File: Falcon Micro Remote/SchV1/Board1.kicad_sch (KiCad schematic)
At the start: 41 parts, among them J41 Conn_01x02_Male, J51 Conn_01x03_Male, SW31 SW_Push, SW51 SW_Push, SW61 SW_Push, SW62 SW_Push, SW63 SW_Push, SW64 SW_Push, SW71 SW_Push, SW72 SW_Push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

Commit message: Made modifications to sch and brd files
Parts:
- D41: footprint (none) -> Diode_SMD:D_SMA
- J41: footprint (none) -> Connector_PinSocket_2.54mm:PinSocket_1x02_P2.54mm_Vertical
- R41, R42: footprint (none) -> Resistor_SMD:R_0402_1005Metric
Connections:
- net B: no longer U2.28 (IO17)
- net F: no longer U2.27 (IO16)
- net L: no longer U2.30 (IO18)
- net L1: no longer R74.1, SW74.2
- net L2: no longer R75.1, SW75.2
- net R: no longer U2.31 (IO19)
- net R1: no longer R71.1, SW71.2
- net LT renamed 23
- net 23: now also U2.37 (IO23)
- net R2 renamed 17
- net 17: now also U2.28 (IO17); no longer U2.36 (IO22)
- net RT renamed 18
- net 18: now also U2.30 (IO18); no longer U2.37 (IO23)
- new net 16: R71.1, SW71.2, U2.27 (IO16)
- new net 19: R74.1, SW74.2, U2.31 (IO19)
- new net 22: R75.1, SW75.2, U2.36 (IO22)
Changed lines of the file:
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@@
     )
   )
-  (global_label "R2" (shape input) (at 60.96 118.745 0) (fields_autoplaced)
-    (effects (font (size 1.27 1.27)) (justify left))
-    (property "Intersheet References" "${INTERSHEET_REFS}" (id 0) (at 65.8526 118.6656 0)
-      (effects (font (size 1.27 1.27)) (justify left) hide)
-    )
-  )
-  (global_label "LT" (shape input) (at 264.16 123.19 0) (fields_autoplaced)
-    (effects (font (size 1.27 1.27)) (justify left))
-    (property "Intersheet References" "${INTERSHEET_REFS}" (id 0) (at 268.5688 123.1106 0)
+  (global_label "22" (shape input) (at 60.96 118.745 0) (fields_autoplaced)
+    (effects (font (size 1.27 1.27)) (justify left))
+    (property "Intersheet References" "${INTERSHEET_REFS}" (id 0) (at 65.7921 118.6656 0)
+      (effects (font (size 1.27 1.27)) (justify left) hide)
+    )
+  )
+  (global_label "23" (shape input) (at 264.16 123.19 0) (fields_autoplaced)
+    (effects (font (size 1.27 1.27)) (justify left))
+    (property "Intersheet References" "${INTERSHEET_REFS}" (id 0) (at 268.9921 123.1106 0)
       (effects (font (size 1.27 1.27)) (justify left) hide)
     )
@@
     )
   )
-  (global_label "R2" (shape input) (at 264.16 53.34 0) (fields_autoplaced)
-    (effects (font (size 1.27 1.27)) (justify left))
-    (property "Intersheet References" "${INTERSHEET_REFS}" (id 0) (at 269.0526 53.2606 0)
+  (global_label "17" (shape input) (at 264.16 53.34 0) (fields_autoplaced)
+    (effects (font (size 1.27 1.27)) (justify left))
+    (property "Intersheet References" "${INTERSHEET_REFS}" (id 0) (at 268.9921 53.2606 0)
       (effects (font (size 1.27 1.27)) (justify left) hide)
     )
@@
     )
   )
-  (global_label "RT" (shape input) (at 264.16 71.755 0) (fields_autoplaced)
-    (effects (font (size 1.27 1.27)) (justify left))
-    (property "Intersheet References" "${INTERSHEET_REFS}" (id 0) (at 268.8107 71.6756 0)
-      (effects (font (size 1.27 1.27)) (justify left) hide)
-    )
-  )
-  (global_label "F" (shape input) (at 60.96 106.045 0) (fields_autoplaced)
-    (effects (font (size 1.27 1.27)) (justify left))
-    (property "Intersheet References" "${INTERSHEET_REFS}" (id 0) (at 64.4617 105.9656 0)
+  (global_label "18" (shape input) (at 264.16 71.755 0) (fields_autoplaced)
+    (effects (font (size 1.27 1.27)) (justify left))
+    (property "Intersheet References" "${INTERSHEET_REFS}" (id 0) (at 268.9921 71.6756 0)
+      (effects (font (size 1.27 1.27)) (justify left) hide)
+    )
+  )
+  (global_label "16" (shape input) (at 60.96 106.045 0) (fields_autoplaced)
+    (effects (font (size 1.27 1.27)) (justify left))
+    (property "Intersheet References" "${INTERSHEET_REFS}" (id 0) (at 65.7921 105.9656 0)
       (effects (font (size 1.27 1.27)) (justify left) hide)
     )
@@
     )
   )
-  (global_label "RT" (shape input) (at 60.96 121.285 0) (fields_autoplaced)
-    (effects (font (size 1.27 1.27)) (justify left))
-    (property "Intersheet References" "${INTERSHEET_REFS}" (id 0) (at 65.6107 121.2056 0)
+  (global_label "23" (shape input) (at 60.96 121.285 0) (fields_autoplaced)
+    (effects (font (size 1.27 1.27)) (justify left))
+    (property "Intersheet References" "${INTERSHEET_REFS}" (id 0) (at 65.7921 121.2056 0)
       (effects (font (size 1.27 1.27)) (justify left) hide)
     )
@@
     )
   )
-  (global_label "L1" (shape input) (at 264.16 88.9 0) (fields_autoplaced)
-    (effects (font (size 1.27 1.27)) (justify left))
-    (property "Intersheet References" "${INTERSHEET_REFS}" (id 0) (at 268.8107 88.8206 0)
+  (global_label "19" (shape input) (at 264.16 88.9 0) (fields_autoplaced)
+    (effects (font (size 1.27 1.27)) (justify left))
+    (property "Intersheet References" "${INTERSHEET_REFS}" (id 0) (at 268.9921 88.8206 0)
       (effects (font (size 1.27 1.27)) (justify left) hide)
     )
@@
     )
   )
-  (global_label "R" (shape input) (at 60.96 113.665 0) (fields_autoplaced)
-    (effects (font (size 1.27 1.27)) (justify left))
-    (property "Intersheet References" "${INTERSHEET_REFS}" (id 0) (at 64.6431 113.5856 0)
+  (global_label "19" (shape input) (at 60.96 113.665 0) (fields_autoplaced)
+    (effects (font (size 1.27 1.27)) (justify left))
+    (property "Intersheet References" "${INTERSHEET_REFS}" (id 0) (at 65.7921 113.5856 0)
       (effects (font (size 1.27 1.27)) (justify left) hide)
     )
@@
     )
   )
-  (global_label "B" (shape input) (at 60.96 108.585 0) (fields_autoplaced)
-    (effects (font (size 1.27 1.27)) (justify left))
-    (property "Intersheet References" "${INTERSHEET_REFS}" (id 0) (at 64.6431 108.5056 0)
-      (effects (font (size 1.27 1.27)) (justify left) hide)
-    )
-  )
-  (global_label "R1" (shape input) (at 264.16 34.925 0) (fields_autoplaced)
-    (effects (font (size 1.27 1.27)) (justify left))
-    (property "Intersheet References" "${INTERSHEET_REFS}" (id 0) (at 269.0526 34.8456 0)
+  (global_label "17" (shape input) (at 60.96 108.585 0) (fields_autoplaced)
+    (effects (font (size 1.27 1.27)) (justify left))
+    (property "Intersheet References" "${INTERSHEET_REFS}" (id 0) (at 65.7921 108.5056 0)
+      (effects (font (size 1.27 1.27)) (justify left) hide)
+    )
+  )
+  (global_label "16" (shape input) (at 264.16 34.925 0) (fields_autoplaced)
+    (effects (font (size 1.27 1.27)) (justify left))
+    (property "Intersheet References" "${INTERSHEET_REFS}" (id 0) (at 268.9921 34.8456 0)
       (effects (font (size 1.27 1.27)) (justify left) hide)
     )
@@
     )
   )
-  (global_label "L" (shape input) (at 60.96 111.125 0) (fields_autoplaced)
-    (effects (font (size 1.27 1.27)) (justify left))
-    (property "Intersheet References" "${INTERSHEET_REFS}" (id 0) (at 64.4012 111.0456 0)
+  (global_label "18" (shape input) (at 60.96 111.125 0) (fields_autoplaced)
+    (effects (font (size 1.27 1.27)) (justify left))
+    (property "Intersheet References" "${INTERSHEET_REFS}" (id 0) (at 65.7921 111.0456 0)
       (effects (font (size 1.27 1.27)) (justify left) hide)
     )
@@
     )
   )
-  (global_label "L2" (shape input) (at 264.16 106.045 0) (fields_autoplaced)
-    (effects (font (size 1.27 1.27)) (justify left))
-    (property "Intersheet References" "${INTERSHEET_REFS}" (id 0) (at 268.8107 105.9656 0)
+  (global_label "22" (shape input) (at 264.16 106.045 0) (fields_autoplaced)
+    (effects (font (size 1.27 1.27)) (justify left))
+    (property "Intersheet References" "${INTERSHEET_REFS}" (id 0) (at 268.9921 105.9656 0)
       (effects (font (size 1.27 1.27)) (justify left) hide)
     )
@@
     (property "Reference" "J41" (id 0) (at 81.28 105.41 0))
     (property "Value" "Conn_01x02_Male" (id 1) (at 81.28 107.95 0))
-    (property "Footprint" "" (id 2) (at 80.645 110.49 0)
+    (property "Footprint" "Connector_PinSocket_2.54mm:PinSocket_1x02_P2.54mm_Vertical" (id 2) (at 80.645 110.49 0)
       (effects (font (size 1.27 1.27)) hide)
     )
@@
       (effects (font (size 1.27 1.27)) (justify left))
     )
-    (property "Footprint" "" (id 2) (at 94.615 102.87 0)
+    (property "Footprint" "Diode_SMD:D_SMA" (id 2) (at 94.615 102.87 0)
       (effects (font (size 1.27 1.27)) hide)
     )
@@
     (property "Reference" "R41" (id 0) (at 85.725 123.825 90))
     (property "Value" "20K" (id 1) (at 85.725 126.365 90))
-    (property "Footprint" "" (id 2) (at 85.725 131.318 90)
+    (property "Footprint" "Resistor_SMD:R_0402_1005Metric" (id 2) (at 85.725 131.318 90)
       (effects (font (size 1.27 1.27)) hide)
     )
@@
     (property "Reference" "R42" (id 0) (at 95.885 123.825 90))
     (property "Value" "1K" (id 1) (at 95.885 126.365 90))
-    (property "Footprint" "" (id 2) (at 95.885 131.318 90)
+    (property "Footprint" "Resistor_SMD:R_0402_1005Metric" (id 2) (at 95.885 131.318 90)
       (effects (font (size 1.27 1.27)) hide)
     )
@@
     )
     (path "/31b509ac-5fa9-466b-884b-c44055794771"
-      (reference "D41") (unit 1) (value "SS34") (footprint "")
+      (reference "D41") (unit 1) (value "SS34") (footprint "Diode_SMD:D_SMA")
     )
     (path "/5251da4a-69d3-4bed-9f5a-6273a802e449"
@@
     )
     (path "/281666d8-effc-4a86-a3e2-2991109dd1f7"
-      (reference "J41") (unit 1) (value "Conn_01x02_Male") (footprint "")
+      (reference "J41") (unit 1) (value "Conn_01x02_Male") (footprint "Connector_PinSocket_2.54mm:PinSocket_1x02_P2.54mm_Vertical")
     )
     (path "/ef5c3a34-7063-439c-a62f-e3d4ec33d429"
@@
     )
     (path "/73fe9c61-cae0-4104-9fd8-66e79eeed8a9"
-      (reference "R41") (unit 1) (value "20K") (footprint "")
+      (reference "R41") (unit 1) (value "20K") (footprint "Resistor_SMD:R_0402_1005Metric")
     )
     (path "/fed00af4-4f5e-4cb3-a3b2-fcebd97f254a"
-      (reference "R42") (unit 1) (value "1K") (footprint "")
+      (reference "R42") (unit 1) (value "1K") (footprint "Resistor_SMD:R_0402_1005Metric")
     )
     (path "/00cc870b-6f65-4413-9723-669a452dccfc"

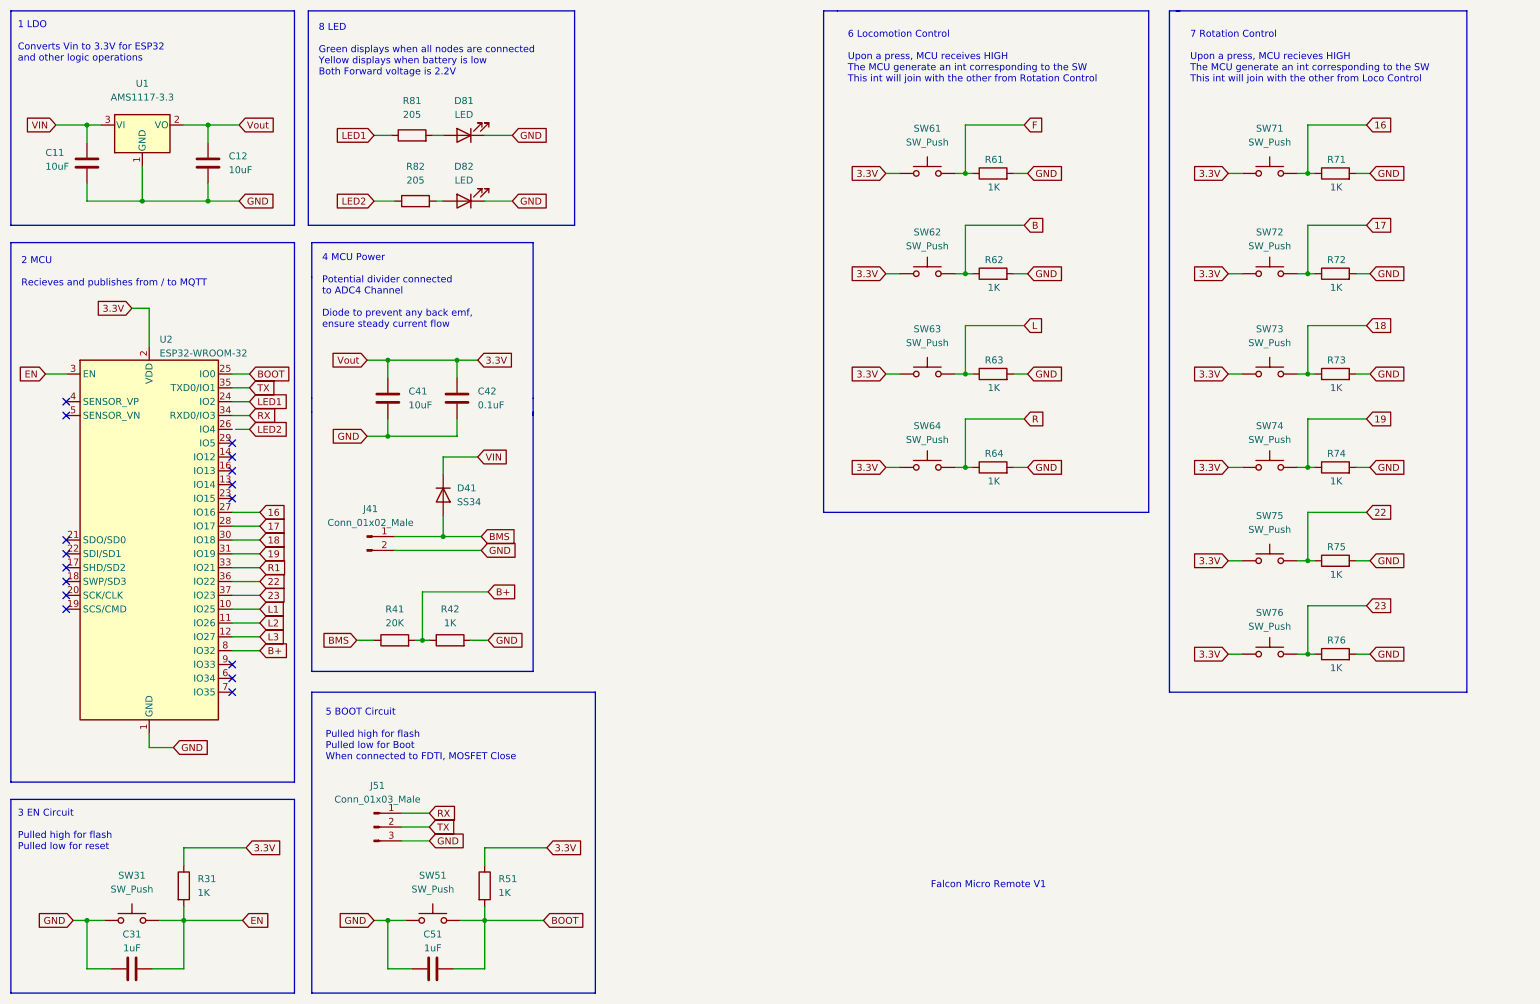
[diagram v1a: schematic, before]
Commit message: Remote V1 has been sent for fabrication, fab project completed Will start on falcon Mini Lab V3, and Remote V2 next iteration
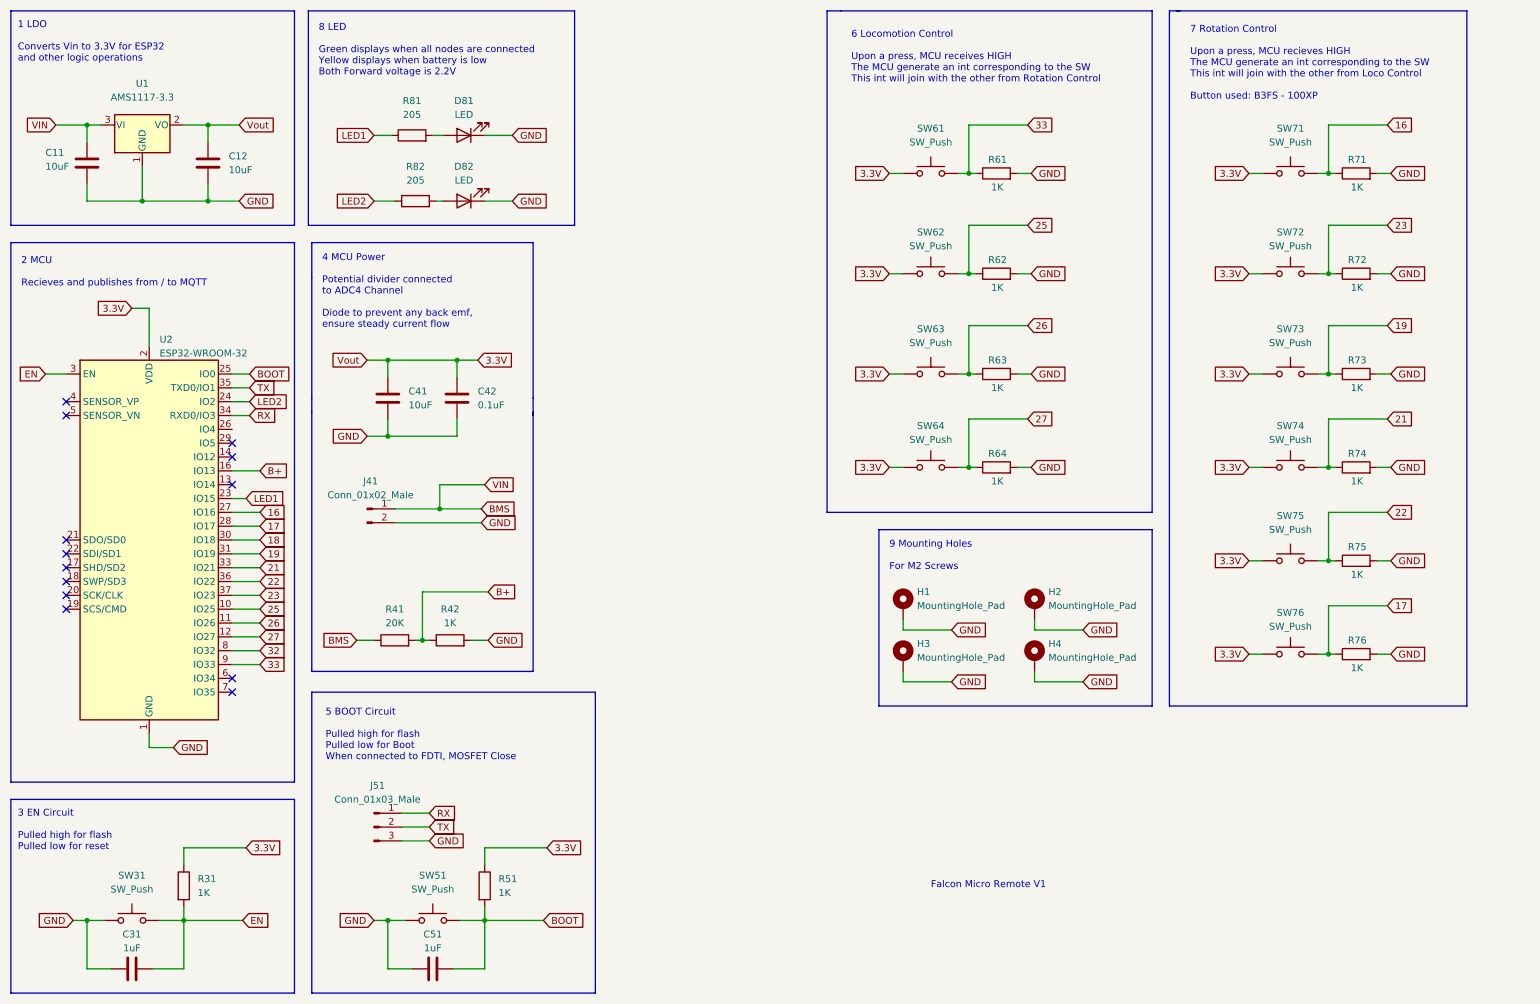
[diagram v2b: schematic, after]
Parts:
- removed D41: SS34, Diode_SMD:D_SMA, symbol Device:D
- added H1, H2, H3, H4: MountingHole_Pad, MountingHole:MountingHole_2.2mm_M2_DIN965_Pad, symbol Mechanical:MountingHole_Pad
- SW31, SW51, SW61, SW62, SW63, SW64, SW71, SW72, SW73, SW74, SW75, SW76: footprint Button_Switch_SMD:SW_SPST_Omron_B3FS-100xP -> Button_Switch_SMD:SW_SPST_PTS645
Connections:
- net F is gone; now on net 33: R61.1, SW61.2
- net L1 is gone; now on net 25: U2.10 (IO25)
- net L2 is gone; now on net 26: U2.11 (IO26)
- net R is gone; now on net 27: R64.1, SW64.2
- net VIN is gone; now on net BMS: C11.1, U1.3 (VI)
- net 17: now also R76.1, SW76.2; no longer R72.1, SW72.2
- net 18: no longer R73.1, SW73.2
- net 19: now also R73.1, SW73.2; no longer R74.1, SW74.2
- net 23: now also R72.1, SW72.2; no longer R76.1, SW76.2
- net B+: now also U2.16 (IO13); no longer U2.8 (IO32)
- net GND: now also H1.1, H2.1, H3.1, H4.1
- net LED1: now also U2.23 (IO15); no longer U2.24 (IO2)
- net LED2: now also U2.24 (IO2)
- net 33: now reaches U2.9 (IO33)
- net B renamed 25
- net L renamed 26
- net L3 renamed 27
- net R1 renamed 21
- net 21: now also R74.1, SW74.2
- new net 32: U2.8 (IO32)
- no-connect marks 16 -> 13
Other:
- note added: "7 Rotation Control Upon a press, MCU recieves HIGH The MCU generate an int corresponding to the SW This int will join with the other from Loco Control Button used: B3FS - 100XP"
- note added: "9 Mounting Holes For M2 Screws"
- note removed: "7 Rotation Control Upon a press, MCU recieves HIGH The MCU generate an int corresponding to the SW This int will join with the other from Loco Control"
- moved on the sheet: J41, R61, R62, R63, R64, R71, R72, R73, R74, R75, R76, SW61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
